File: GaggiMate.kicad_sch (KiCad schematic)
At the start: 16 parts, among them J1 Heater SSR, J2 Pump relay, J3 K-Type probe, J4 Valve relay, J5 Pressure Sensor, J6 Brew BTN, J7 Steam BTN, J8 SW_DEBUG_PINS, J9 Loadcell?, P1 USB_C_Plug_USB2.0, U1 ESP32-S3-WROOM-1, U2 MAX31855KASA, U3 ADS1115IDGS

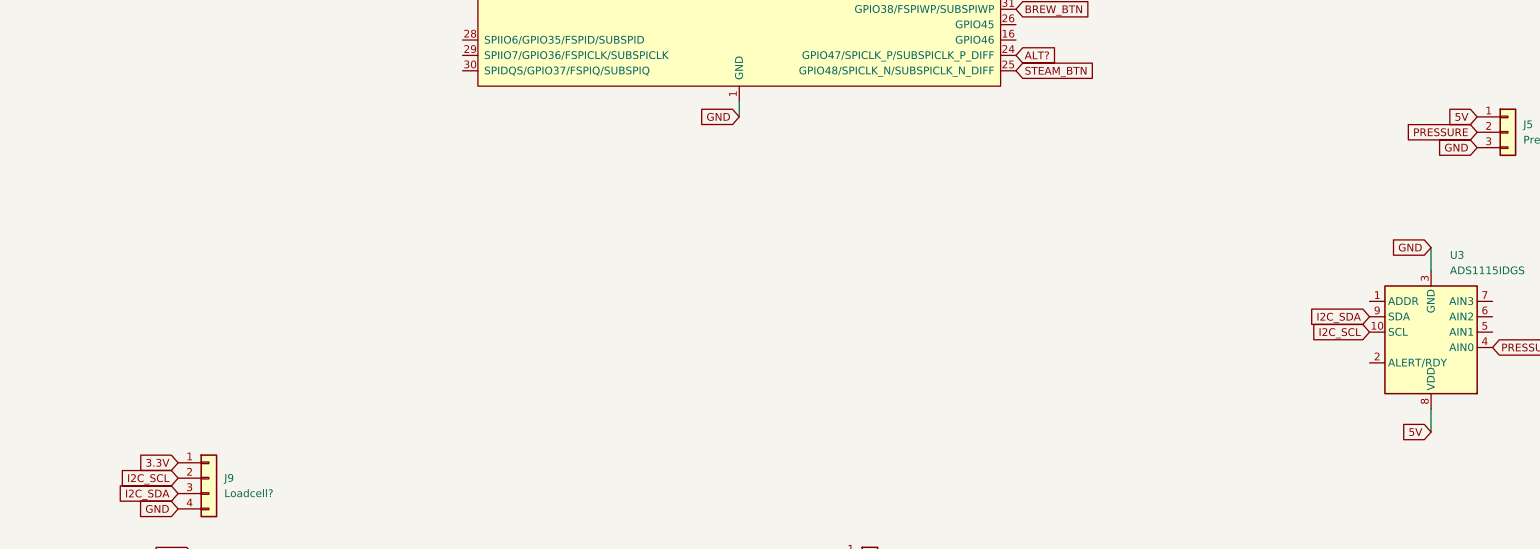
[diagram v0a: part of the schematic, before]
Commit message: updated power and began 5-3v regulator
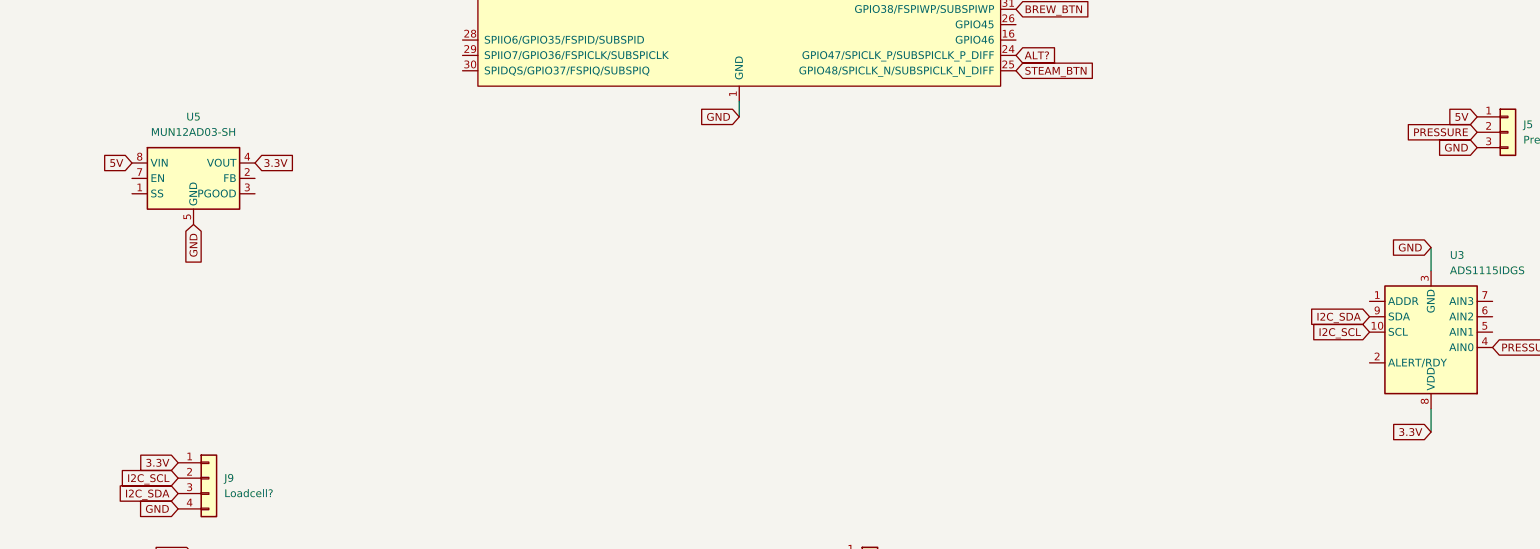
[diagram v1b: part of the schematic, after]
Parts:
- added U5: MUN12AD03-SH, Converter_DCDC:Converter_DCDC_Cyntec_MUN12AD03-SH, symbol Regulator_Switching:MUN12AD03-SH
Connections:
- net 3.3V: now also U3.8 (VDD), U5.4 (VOUT), U5.9 (VOUT)
- net 5V: now also U5.8 (VIN); no longer U3.8 (VDD)
- net GND: now also U5.10 (GND), U5.11 (GND), U5.5 (GND)

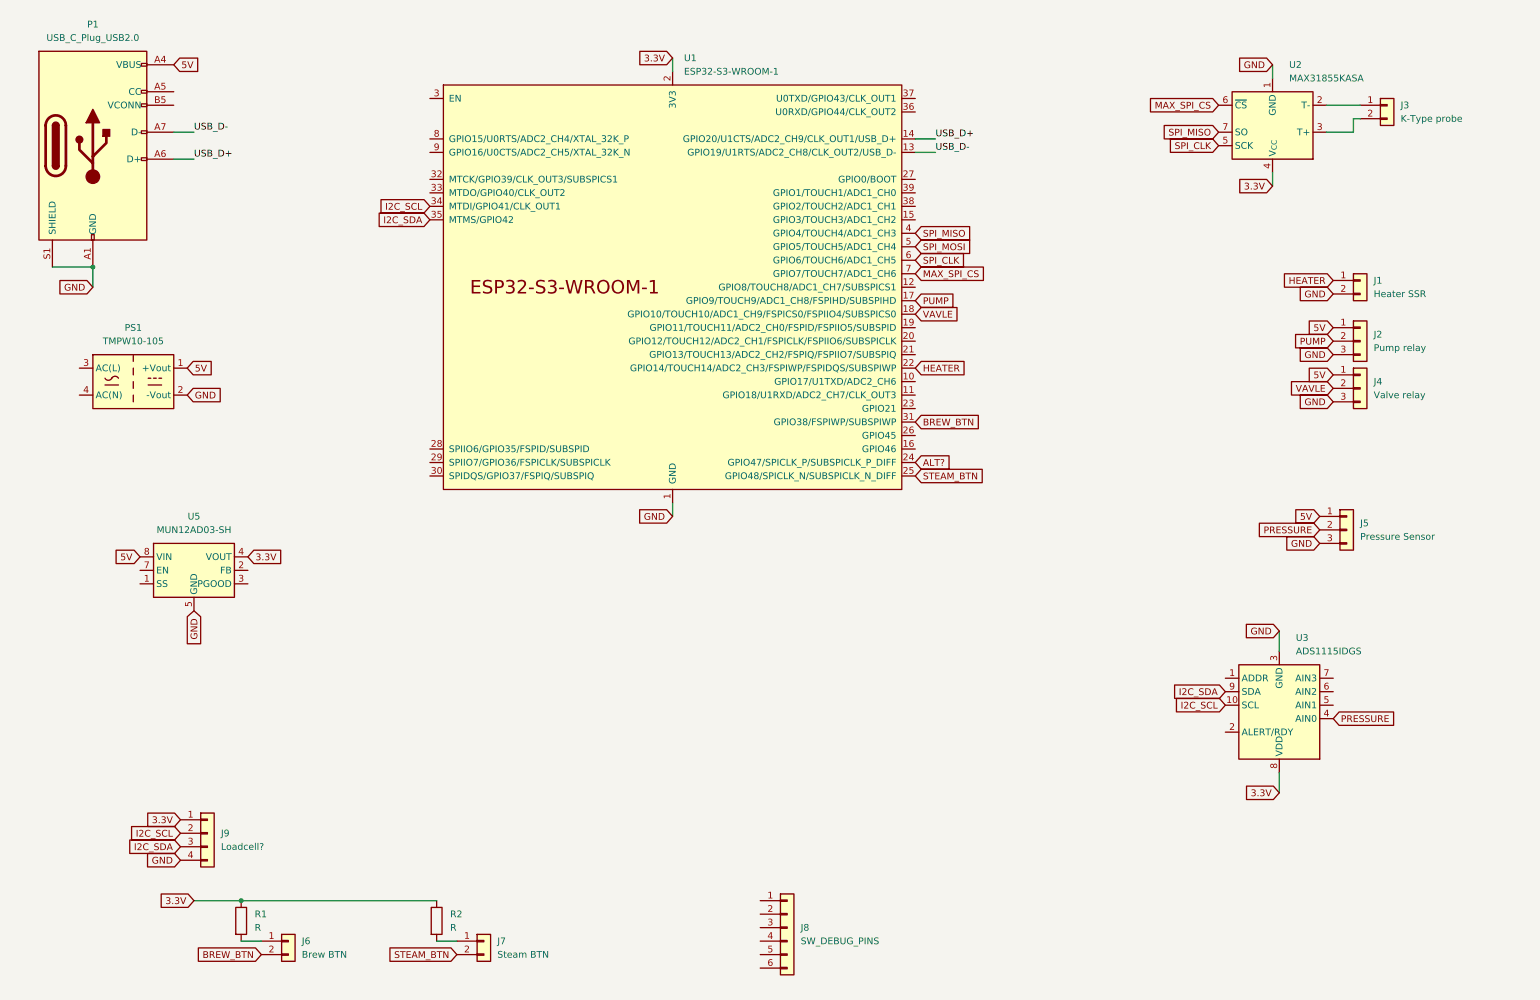
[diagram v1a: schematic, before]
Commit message: bunch of updates
added:
- relays
- barrel jack
- more proper routing
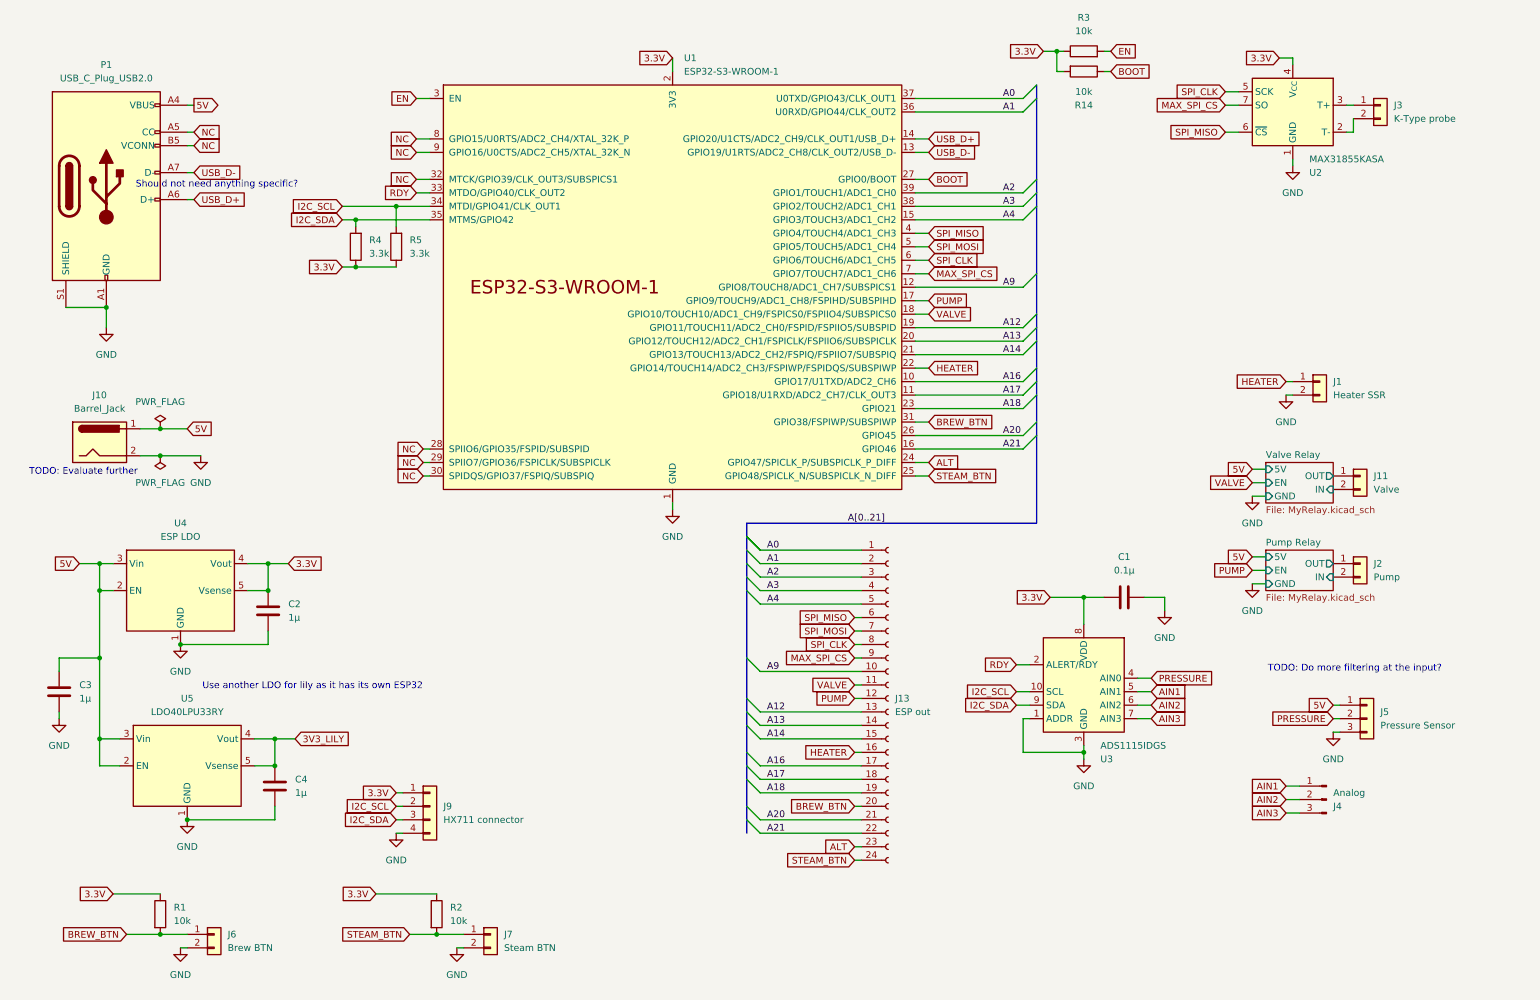
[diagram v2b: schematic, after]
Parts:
- removed J2: Pump relay, symbol Connector_Generic:Conn_01x03
- removed J4: Valve relay, symbol Connector_Generic:Conn_01x03
- removed J8: SW_DEBUG_PINS, symbol Connector_Generic:Conn_01x06
- removed PS1: TMPW10-105, Converter_ACDC:Converter_ACDC_TRACO_TMPW10_1xx_THT, symbol Converter_ACDC:TMPW10-105
- removed U5: MUN12AD03-SH, Converter_DCDC:Converter_DCDC_Cyntec_MUN12AD03-SH, symbol Regulator_Switching:MUN12AD03-SH
- added C1: 0.1µ, symbol Device:C
- added C2, C3, C4: 1µ, symbol Device:C
- added J10: Barrel_Jack, symbol Connector:Barrel_Jack
- added J11: Valve, symbol Connector_Generic:Conn_01x02
- added J13: ESP out, symbol Connector:Conn_01x24_Socket
- added J2: Pump, symbol Connector_Generic:Conn_01x02
- added J4: Analog, symbol Connector:Conn_01x03_Pin
- added R14, R3: 10k, Resistor_SMD:R_0201_0603Metric, symbol Device:R
- added R4, R5: 3.3k, Resistor_SMD:R_0201_0603Metric, symbol Device:R
- added U4: ESP LDO, Package_DFN_QFN:DFN-6-1EP_3x3mm_P0.95mm_EP1.7x2.6mm, symbol Regulator_Linear:LDO40LPU33RY
- added U5: LDO40LPU33RY, Package_DFN_QFN:DFN-6-1EP_3x3mm_P0.95mm_EP1.7x2.6mm, symbol Regulator_Linear:LDO40LPU33RY
- J9: value Loadcell? -> HX711 connector
- R1, R2: value R -> 10k; footprint (none) -> Resistor_SMD:R_0201_0603Metric
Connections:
- net 3.3V: now also C1.1, C2.1, R14.2, R3.1, R4.1, R5.1, U4.4 (Vout), U4.5 (Vsense)
- net 5V: now also C3.2, J10.1, U4.2 (EN), U4.3 (Vin), U5.2 (EN), U5.3 (Vin)
- net BREW_BTN: now also J6.1 (Pin_1), R1.2, J13.20 (Pin_20); no longer J6.2 (Pin_2)
- net GND: now also J6.2 (Pin_2), J7.2 (Pin_2), U3.1 (ADDR), C1.2, C2.2, C3.1, C4.2, J10.2, U4.1 (GND), U4.7 (GND), U5.1 (GND), U5.7 (GND)
- net HEATER: now also J13.16 (Pin_16)
- net I2C_SCL: now also R5.2
- net I2C_SDA: now also R4.2
- net MAX_SPI_CS: now also U2.7 (SO), J13.9 (Pin_9); no longer U2.6 (~{CS})
- net PUMP: now also J13.12 (Pin_12)
- net SPI_CLK: now also J13.8 (Pin_8)
- net SPI_MISO: now also U2.6 (~{CS}), J13.6 (Pin_6); no longer U2.7 (SO)
- net SPI_MOSI: now also J13.7 (Pin_7)
- net STEAM_BTN: now also J7.1 (Pin_1), R2.2, J13.24 (Pin_24); no longer J7.2 (Pin_2)
- net RDY: now reaches U3.2 (ALERT/RDY)
- net RDY: now also U1.33 (MTDO/GPIO40/CLK_OUT2)
- net AIN1: now reaches U3.5 (AIN1)
- net AIN1: now also J4.1 (Pin_1)
- net AIN2: now reaches U3.6 (AIN2)
- net AIN2: now also J4.2 (Pin_2)
- net AIN3: now reaches U3.7 (AIN3)
- net AIN3: now also J4.3 (Pin_3)
- net at U2.2 (T-): now also J3.2 (Pin_2); no longer J3.1 (Pin_1)
- net at U2.3 (T+): now also J3.1 (Pin_1); no longer J3.2 (Pin_2)
- net A16: now reaches U1.10 (GPIO17/U1TXD/ADC2_CH6)
- net A16: now also J13.17 (Pin_17)
- net A17: now reaches U1.11 (GPIO18/U1RXD/ADC2_CH7/CLK_OUT3)
- net A17: now also J13.18 (Pin_18)
- net A9: now reaches U1.12 (GPIO8/TOUCH8/ADC1_CH7/SUBSPICS1)
- net A9: now also J13.10 (Pin_10)
- net A4: now reaches U1.15 (GPIO3/TOUCH3/ADC1_CH2)
- net A4: now also J13.5 (Pin_5)
- net A21: now reaches U1.16 (GPIO46)
- net A21: now also J13.22 (Pin_22)
- net A12: now reaches U1.19 (GPIO11/TOUCH11/ADC2_CH0/FSPID/FSPIIO5/SUBSPID)
- net A12: now also J13.13 (Pin_13)
- net A13: now reaches U1.20 (GPIO12/TOUCH12/ADC2_CH1/FSPICLK/FSPIIO6/SUBSPICLK)
- net A13: now also J13.14 (Pin_14)
- net A14: now reaches U1.21 (GPIO13/TOUCH13/ADC2_CH2/FSPIQ/FSPIIO7/SUBSPIQ)
- net A14: now also J13.15 (Pin_15)
- net A18: now reaches U1.23 (GPIO21)
- net A18: now also J13.19 (Pin_19)
- net A20: now reaches U1.26 (GPIO45)
- net A20: now also J13.21 (Pin_21)
- net BOOT: now reaches U1.27 (GPIO0/BOOT)
- net BOOT: now also R14.1
- net NC: now reaches U1.28 (SPIIO6/GPIO35/FSPID/SUBSPID)
- net NC: now also P1.A5 (CC), P1.B5 (VCONN), U1.29 (SPIIO7/GPIO36/FSPICLK/SUBSPICLK), U1.30 (SPIDQS/GPIO37/FSPIQ/SUBSPIQ), U1.32 (MTCK/GPIO39/CLK_OUT3/SUBSPICS1), U1.8 (GPIO15/U0RTS/ADC2_CH4/XTAL_32K_P), U1.9 (GPIO16/U0CTS/ADC2_CH5/XTAL_32K_N)
- net EN: now reaches U1.3 (EN)
- net EN: now also R3.2
- net A1: now reaches U1.36 (U0RXD/GPIO44/CLK_OUT2)
- net A1: now also J13.2 (Pin_2)
- net A0: now reaches U1.37 (U0TXD/GPIO43/CLK_OUT1)
- net A0: now also J13.1 (Pin_1)
- net A3: now reaches U1.38 (GPIO2/TOUCH2/ADC1_CH1)
- net A3: now also J13.4 (Pin_4)
- net A2: now reaches U1.39 (GPIO1/TOUCH1/ADC1_CH0)
- net A2: now also J13.3 (Pin_3)
- net ALT? renamed ALT
- net ALT: now also J13.23 (Pin_23)
- net VAVLE renamed VALVE
- net VALVE: now also J13.11 (Pin_11)
- new net 3V3_LILY: C4.1, U5.4 (Vout), U5.5 (Vsense)
- new net Pump Relay/IN: J2.2 (Pin_2)
- new net Pump Relay/OUT: J2.1 (Pin_1)
- new net Valve Relay/IN: J11.2 (Pin_2)
- new net Valve Relay/OUT: J11.1 (Pin_1)
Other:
- added sheet Pump Relay (MyRelay.kicad_sch)
- added sheet Valve Relay (MyRelay.kicad_sch)
- note added: "Should not need anything specific?"
- note added: "TODO: Do more filtering at the input?"
- note added: "TODO: Evaluate further"
- note added: "Use another LDO for lily as it has its own ESP32"
- moved on the sheet: J1, J3, J5, J6, J7, J9, P1, R1, R2, U2, U3

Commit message: attempt a HV stepdown and some PCB stuff
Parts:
- removed C4: 1µ, symbol Device:C
- removed J10: Barrel_Jack, symbol Connector:Barrel_Jack
- removed J11: Valve, symbol Connector_Generic:Conn_01x02
- removed J2: Pump, symbol Connector_Generic:Conn_01x02
- removed U4: ESP LDO, Package_DFN_QFN:DFN-6-1EP_3x3mm_P0.95mm_EP1.7x2.6mm, symbol Regulator_Linear:LDO40LPU33RY
- removed U5: LDO40LPU33RY, Package_DFN_QFN:DFN-6-1EP_3x3mm_P0.95mm_EP1.7x2.6mm, symbol Regulator_Linear:LDO40LPU33RY
- added H1: HV_N, symbol Mechanical:MountingHole_Pad
- added H2: HV_L, symbol Mechanical:MountingHole_Pad
- added J2: HV_VALVE, symbol Connector_Generic:Conn_01x01
- added J8: HV_PUMP, symbol Connector_Generic:Conn_01x01
- added U4: AMS1117-3.3, Package_TO_SOT_SMD:SOT-223-3_TabPin2, symbol Regulator_Linear:AMS1117-3.3
- C2, C3: value 1µ -> 10µ
- J13: footprint (none) -> Connector_PinHeader_2.54mm:PinHeader_1x24_P2.54mm_Vertical_SMD_Pin1Right
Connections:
- net 3.3V: now also U4.2 (VO)
- net 5V: now also C3.1, U4.3 (VI); no longer C3.2
- net GND: now also C3.2, U4.1 (GND); no longer C3.1
- net Pump Relay/OUT: now also J8.1 (Pin_1)
- net Valve Relay/OUT: now also J2.1 (Pin_1)
- new net HVSupply/N: H1.1
- new net HV_L: H2.1
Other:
- added sheet HVSupply (HVSupply.kicad_sch)
- note removed: "TODO: Evaluate further"
- note removed: "Use another LDO for lily as it has its own ESP32"
- moved on the sheet: C2, J9
